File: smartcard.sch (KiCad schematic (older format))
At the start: 9 parts, among them J2201 Smart_Card, U2201 SEC1110

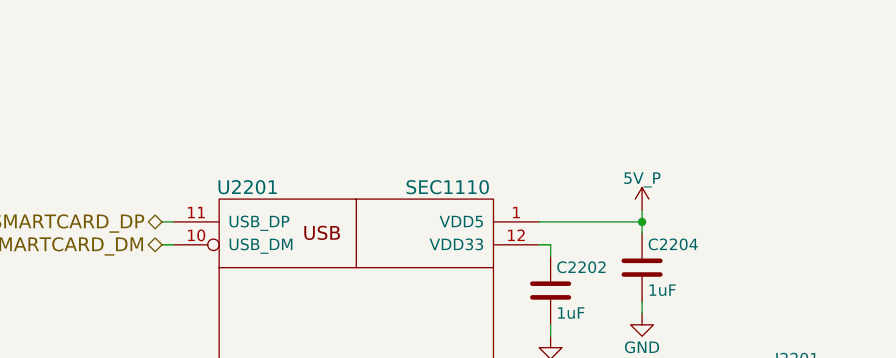
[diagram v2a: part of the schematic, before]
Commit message: Move more symbols, sheets, and pins around on the front sheet to make it even clearer, bring back the old hierarchical structure (again), bring back each sheet's title, add large text "titles" to each sheet reflecting what they are for
Still need to double check everything on the first page.
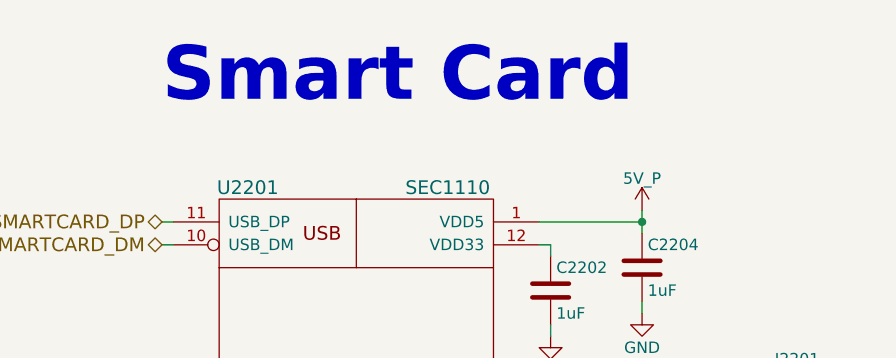
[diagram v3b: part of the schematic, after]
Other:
- note added: "Smart Card"
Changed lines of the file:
@@
 encoding utf-8
 Sheet 22 24
-Title "Librem5 development kit"
+Title "Smart Card"
 Date "2018-06-11"
 Rev "v0.1.0"
@@
 SMARTCARD_DM
 $Comp
-L 5V_P #PWR0249
+L 5V_P #PWR0360
 U 1 1 5B1F0A54
 P 6900 2250
-F 0 "#PWR0249" H 6900 2100 50  0001 C CNN
+F 0 "#PWR0360" H 6900 2100 50  0001 C CNN
 F 1 "5V_P" H 6900 2390 50  0000 C CNN
 F 2 "" H 6900 2250 50  0001 C CNN
@@
 $EndComp
 $Comp
-L GND #PWR0250
+L GND #PWR0361
 U 1 1 5B1F199A
 P 6500 2800
-F 0 "#PWR0250" H 6500 2550 50  0001 C CNN
+F 0 "#PWR0361" H 6500 2550 50  0001 C CNN
 F 1 "GND" H 6500 2650 50  0000 C CNN
 F 2 "" H 6500 2800 50  0001 C CNN
@@
 $EndComp
 $Comp
-L GND #PWR0251
+L GND #PWR0362
 U 1 1 5B1F1D4E
 P 6900 2700
-F 0 "#PWR0251" H 6900 2450 50  0001 C CNN
+F 0 "#PWR0362" H 6900 2450 50  0001 C CNN
 F 1 "GND" H 6900 2550 50  0000 C CNN
 F 2 "" H 6900 2700 50  0001 C CNN
@@
 $EndComp
 $Comp
-L 5V_P #PWR0252
+L 5V_P #PWR0363
 U 1 1 5B20FF3B
 P 4700 3700
-F 0 "#PWR0252" H 4700 3550 50  0001 C CNN
+F 0 "#PWR0363" H 4700 3550 50  0001 C CNN
 F 1 "5V_P" H 4700 3840 50  0000 C CNN
 F 2 "" H 4700 3700 50  0001 C CNN
@@
 $EndComp
 $Comp
-L GND #PWR0253
+L GND #PWR0364
 U 1 1 5B20FFAF
 P 4700 4500
-F 0 "#PWR0253" H 4700 4250 50  0001 C CNN
+F 0 "#PWR0364" H 4700 4250 50  0001 C CNN
 F 1 "GND" H 4700 4350 50  0000 C CNN
 F 2 "" H 4700 4500 50  0001 C CNN
@@
 $EndComp
 $Comp
-L GND #PWR0254
+L GND #PWR0365
 U 1 1 5B210E33
 P 6500 3200
-F 0 "#PWR0254" H 6500 2950 50  0001 C CNN
+F 0 "#PWR0365" H 6500 2950 50  0001 C CNN
 F 1 "GND" H 6500 3050 50  0000 C CNN
 F 2 "" H 6500 3200 50  0001 C CNN
@@
 $EndComp
 $Comp
-L GND #PWR0255
+L GND #PWR0366
 U 1 1 5B21589D
 P 6500 4550
-F 0 "#PWR0255" H 6500 4300 50  0001 C CNN
+F 0 "#PWR0366" H 6500 4300 50  0001 C CNN
 F 1 "GND" H 6500 4400 50  0000 C CNN
 F 2 "" H 6500 4550 50  0001 C CNN
@@
 NoConn ~ 7350 3400
 $Comp
-L GND #PWR0256
+L GND #PWR0367
 U 1 1 5B27C54B
 P 7300 3950
-F 0 "#PWR0256" H 7300 3700 50  0001 C CNN
+F 0 "#PWR0367" H 7300 3700 50  0001 C CNN
 F 1 "GND" H 7300 3800 50  0000 C CNN
 F 2 "" H 7300 3950 50  0001 C CNN
@@
 Normally\nOpen
 $Comp
-L GND #PWR0257
+L GND #PWR0368
 U 1 1 5B296537
 P 8600 3400
-F 0 "#PWR0257" H 8600 3150 50  0001 C CNN
+F 0 "#PWR0368" H 8600 3150 50  0001 C CNN
 F 1 "GND" H 8600 3250 50  0000 C CNN
 F 2 "" H 8600 3400 50  0001 C CNN
@@
 Wire Wire Line
 	4800 2300 4850 2300
+Text Notes 4800 1800 0    236  ~ 47
+Smart Card
 $EndSCHEMATC

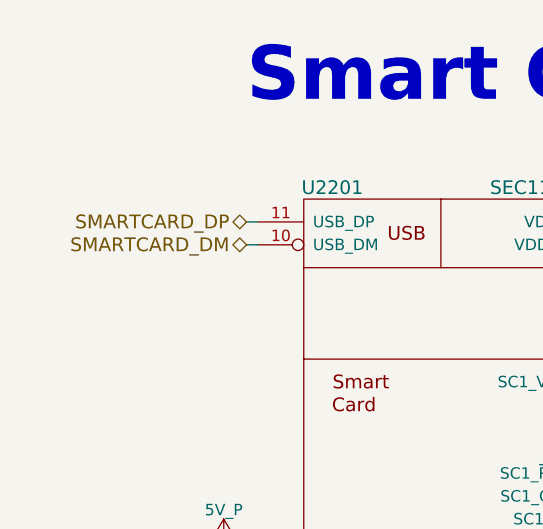
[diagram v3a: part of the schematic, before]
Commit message: Make all differential pair signal names end in P/N so that diff routing works when in layout
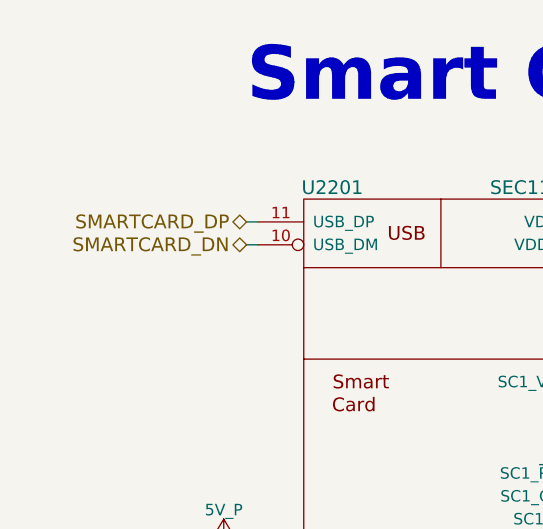
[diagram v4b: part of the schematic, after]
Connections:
- net SMARTCARD_DM renamed SMARTCARD_DN
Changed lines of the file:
@@
 SMARTCARD_DP
 Text HLabel 4800 2400 0    60   BiDi ~ 0
-SMARTCARD_DM
+SMARTCARD_DN
 $Comp
 L 5V_P #PWR0360

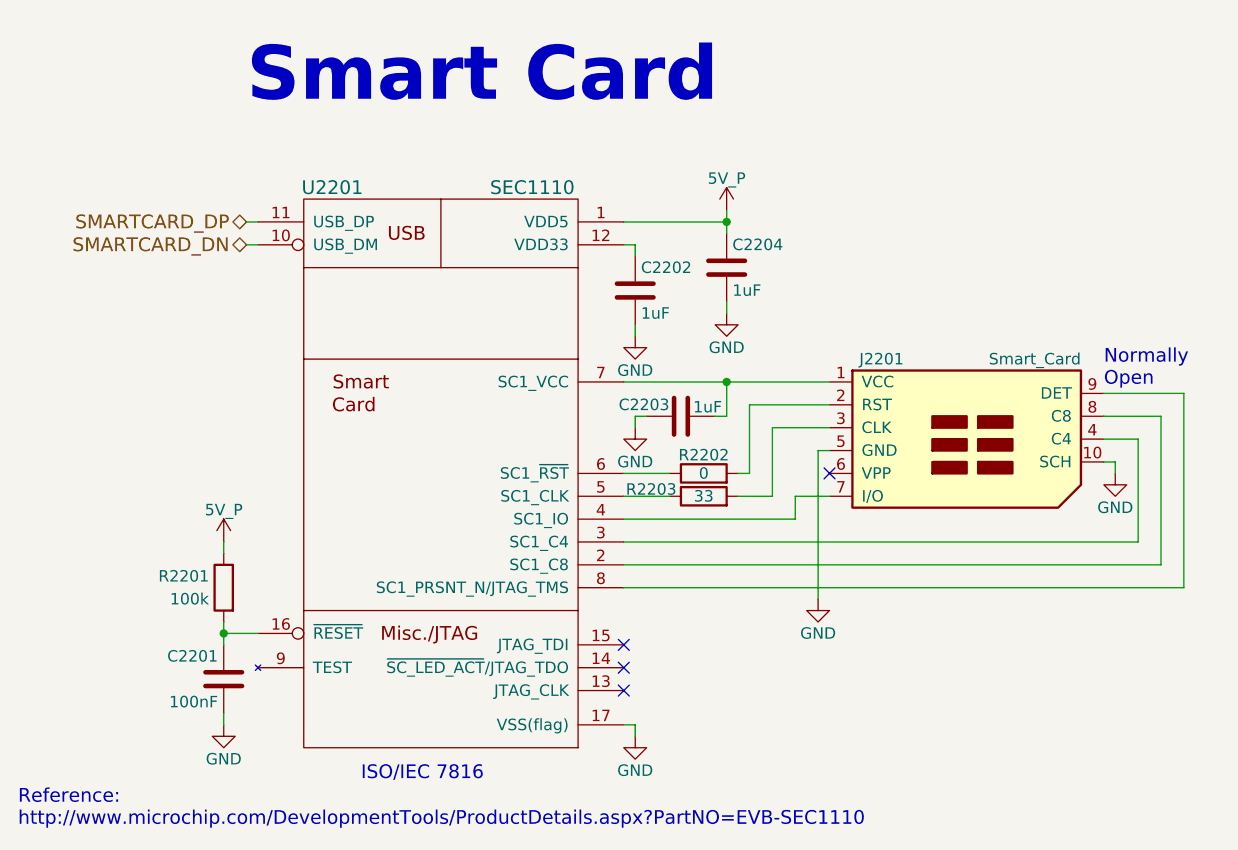
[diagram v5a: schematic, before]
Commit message: Add AC coupling caps to the HDMI_AUXP/N diff pair which were mistakenly left out, fix a couple typos/errors that were made when transitioning to the new top-leve sheet, make the M.2s' I2C RX TX hierarchical signals consistent and clearer
Hopefully all lingering errors have been caught, this will likely be the schematic commit that gets reviewed (fingers crossed).
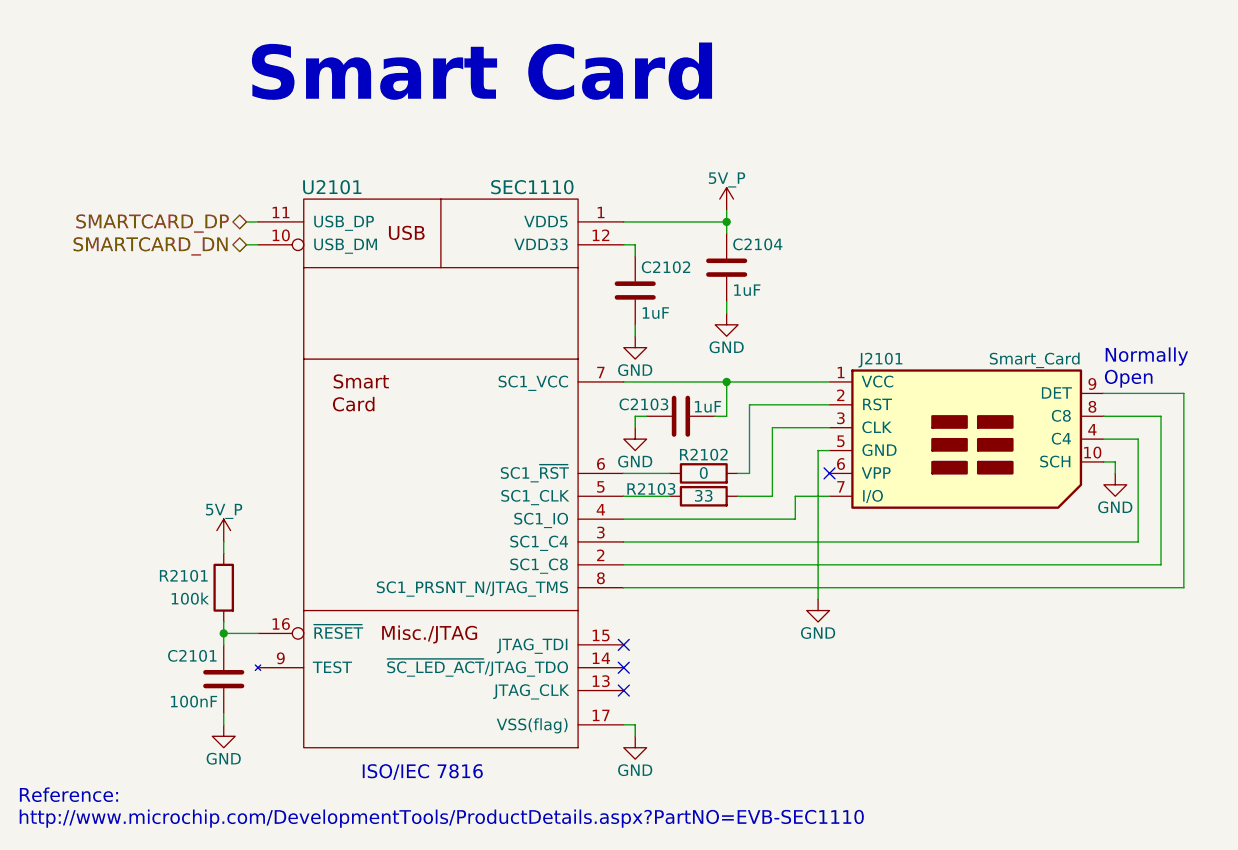
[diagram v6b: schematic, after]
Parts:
- renumbered C2201 to C2101, C2202 to C2102, C2203 to C2103, C2204 to C2104, J2201 to J2101, R2201 to R2101, R2202 to R2102, R2203 to R2103, U2201 to U2101
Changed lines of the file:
@@
 $Descr A4 11693 8268
 encoding utf-8
-Sheet 22 24
+Sheet 21 24
 Title "Smart Card"
 Date "2018-06-14"
@@
 SMARTCARD_DN
 $Comp
-L 5V_P #PWR2206
+L 5V_P #PWR0333
 U 1 1 5B1F0A54
 P 6900 2250
-F 0 "#PWR2206" H 6900 2100 50  0001 C CNN
+F 0 "#PWR0333" H 6900 2100 50  0001 C CNN
 F 1 "5V_P" H 6900 2390 50  0000 C CNN
 F 2 "" H 6900 2250 50  0001 C CNN
@@
 $EndComp
 $Comp
-L C C2202
+L C C2102
 U 1 1 5B1F1971
 P 6500 2600
-F 0 "C2202" H 6525 2700 50  0000 L CNN
+F 0 "C2102" H 6525 2700 50  0000 L CNN
 F 1 "1uF" H 6525 2500 50  0000 L CNN
 F 2 "Capacitors_SMD:C_0603" H 6538 2450 50  0001 C CNN
@@
 $EndComp
 $Comp
-L GND #PWR2203
+L GND #PWR0334
 U 1 1 5B1F199A
 P 6500 2800
-F 0 "#PWR2203" H 6500 2550 50  0001 C CNN
+F 0 "#PWR0334" H 6500 2550 50  0001 C CNN
 F 1 "GND" H 6500 2650 50  0000 C CNN
 F 2 "" H 6500 2800 50  0001 C CNN
@@
 $EndComp
 $Comp
-L C C2204
+L C C2104
 U 1 1 5B1F1CFA
 P 6900 2500
-F 0 "C2204" H 6925 2600 50  0000 L CNN
+F 0 "C2104" H 6925 2600 50  0000 L CNN
 F 1 "1uF" H 6925 2400 50  0000 L CNN
 F 2 "Capacitors_SMD:C_0603" H 6938 2350 50  0001 C CNN
@@
 $EndComp
 $Comp
-L GND #PWR2207
+L GND #PWR0335
 U 1 1 5B1F1D4E
 P 6900 2700
-F 0 "#PWR2207" H 6900 2450 50  0001 C CNN
+F 0 "#PWR0335" H 6900 2450 50  0001 C CNN
 F 1 "GND" H 6900 2550 50  0000 C CNN
 F 2 "" H 6900 2700 50  0001 C CNN
@@
 $EndComp
 $Comp
-L R R2202
+L R R2102
 U 1 1 5B1F2A2C
 P 6800 3400
-F 0 "R2202" V 6880 3400 50  0000 C CNN
+F 0 "R2102" V 6880 3400 50  0000 C CNN
 F 1 "0" V 6800 3400 50  0000 C CNN
 F 2 "Resistors_SMD:R_0603" V 6730 3400 50  0001 C CNN
@@
 $EndComp
 $Comp
-L R R2203
+L R R2103
 U 1 1 5B1F2AD0
 P 6800 3500
-F 0 "R2203" V 6830 3730 50  0000 C CNN
+F 0 "R2103" V 6830 3730 50  0000 C CNN
 F 1 "33" V 6800 3500 50  0000 C CNN
 F 2 "Resistors_SMD:R_0603" V 6730 3500 50  0001 C CNN
@@
 NoConn ~ 6450 4350
 $Comp
-L R R2201
+L R R2101
 U 1 1 5B20FE9D
 P 4700 3900
-F 0 "R2201" H 4875 3950 50  0000 C CNN
+F 0 "R2101" H 4875 3950 50  0000 C CNN
 F 1 "100k" H 4850 3850 50  0000 C CNN
 F 2 "Resistors_SMD:R_0603" V 4630 3900 50  0001 C CNN
@@
 $EndComp
 $Comp
-L 5V_P #PWR2201
+L 5V_P #PWR0336
 U 1 1 5B20FF3B
 P 4700 3700
-F 0 "#PWR2201" H 4700 3550 50  0001 C CNN
+F 0 "#PWR0336" H 4700 3550 50  0001 C CNN
 F 1 "5V_P" H 4700 3840 50  0000 C CNN
 F 2 "" H 4700 3700 50  0001 C CNN
@@
 $EndComp
 $Comp
-L C C2201
+L C C2101
 U 1 1 5B20FF65
 P 4700 4300
-F 0 "C2201" H 4725 4400 50  0000 L CNN
+F 0 "C2101" H 4725 4400 50  0000 L CNN
 F 1 "100nF" H 4725 4200 50  0000 L CNN
 F 2 "Capacitors_SMD:C_0603" H 4738 4150 50  0001 C CNN
@@
 $EndComp
 $Comp
-L GND #PWR2202
+L GND #PWR0337
 U 1 1 5B20FFAF
 P 4700 4500
-F 0 "#PWR2202" H 4700 4250 50  0001 C CNN
+F 0 "#PWR0337" H 4700 4250 50  0001 C CNN
 F 1 "GND" H 4700 4350 50  0000 C CNN
 F 2 "" H 4700 4500 50  0001 C CNN
@@
 $EndComp
 $Comp
-L C C2203
+L C C2103
 U 1 1 5B210DE6
 P 6700 3150
-F 0 "C2203" V 6750 3200 50  0000 L CNN
+F 0 "C2103" V 6750 3200 50  0000 L CNN
 F 1 "1uF" V 6740 2970 50  0000 L CNN
 F 2 "Capacitors_SMD:C_0603" H 6738 3000 50  0001 C CNN
@@
 $EndComp
 $Comp
-L GND #PWR2204
+L GND #PWR0338
 U 1 1 5B210E33
 P 6500 3200
-F 0 "#PWR2204" H 6500 2950 50  0001 C CNN
+F 0 "#PWR0338" H 6500 2950 50  0001 C CNN
 F 1 "GND" H 6500 3050 50  0000 C CNN
 F 2 "" H 6500 3200 50  0001 C CNN
@@
 $EndComp
 $Comp
-L GND #PWR2205
+L GND #PWR0339
 U 1 1 5B21589D
 P 6500 4550
-F 0 "#PWR2205" H 6500 4300 50  0001 C CNN
+F 0 "#PWR0339" H 6500 4300 50  0001 C CNN
 F 1 "GND" H 6500 4400 50  0000 C CNN
 F 2 "" H 6500 4550 50  0001 C CNN
@@
 ISO/IEC 7816
 $Comp
-L SEC1110 U2201
+L SEC1110 U2101
 U 1 1 5B265531
 P 5650 3400
-F 0 "U2201" H 5175 4650 60  0000 C CNN
+F 0 "U2101" H 5175 4650 60  0000 C CNN
 F 1 "SEC1110" H 6050 4650 60  0000 C CNN
 F 2 "" H 5650 3700 60  0001 C CNN
@@
 $EndComp
 $Comp
-L SMART_CARD J2201
+L SMART_CARD J2101
 U 1 1 5B26711A
 P 7850 3300
-F 0 "J2201" H 7675 3700 50  0000 R CNN
+F 0 "J2101" H 7675 3700 50  0000 R CNN
 F 1 "Smart_Card" H 8450 3700 50  0000 R CNN
 F 2 "dvk-mx8m-bsb:Conn_Amphenol_SIMcard_10100271" H 7850 3650 50  0001 C CNN
@@
 NoConn ~ 7350 3400
 $Comp
-L GND #PWR2208
+L GND #PWR0340
 U 1 1 5B27C54B
 P 7300 3950
-F 0 "#PWR2208" H 7300 3700 50  0001 C CNN
+F 0 "#PWR0340" H 7300 3700 50  0001 C CNN
 F 1 "GND" H 7300 3800 50  0000 C CNN
 F 2 "" H 7300 3950 50  0001 C CNN
@@
 Normally\nOpen
 $Comp
-L GND #PWR2209
+L GND #PWR0341
 U 1 1 5B296537
 P 8600 3400
-F 0 "#PWR2209" H 8600 3150 50  0001 C CNN
+F 0 "#PWR0341" H 8600 3150 50  0001 C CNN
 F 1 "GND" H 8600 3250 50  0000 C CNN
 F 2 "" H 8600 3400 50  0001 C CNN
